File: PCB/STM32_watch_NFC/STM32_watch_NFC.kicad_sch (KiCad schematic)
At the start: 54 parts, among them J1 Conn_01x06_Socket, Q1 2N7000, SW1 SW_DPST_x2, SW2 SW_DPST_x2, SW3 SW_DPST_x2, U1 STM32L031G6Ux, Y2 32.768kHz

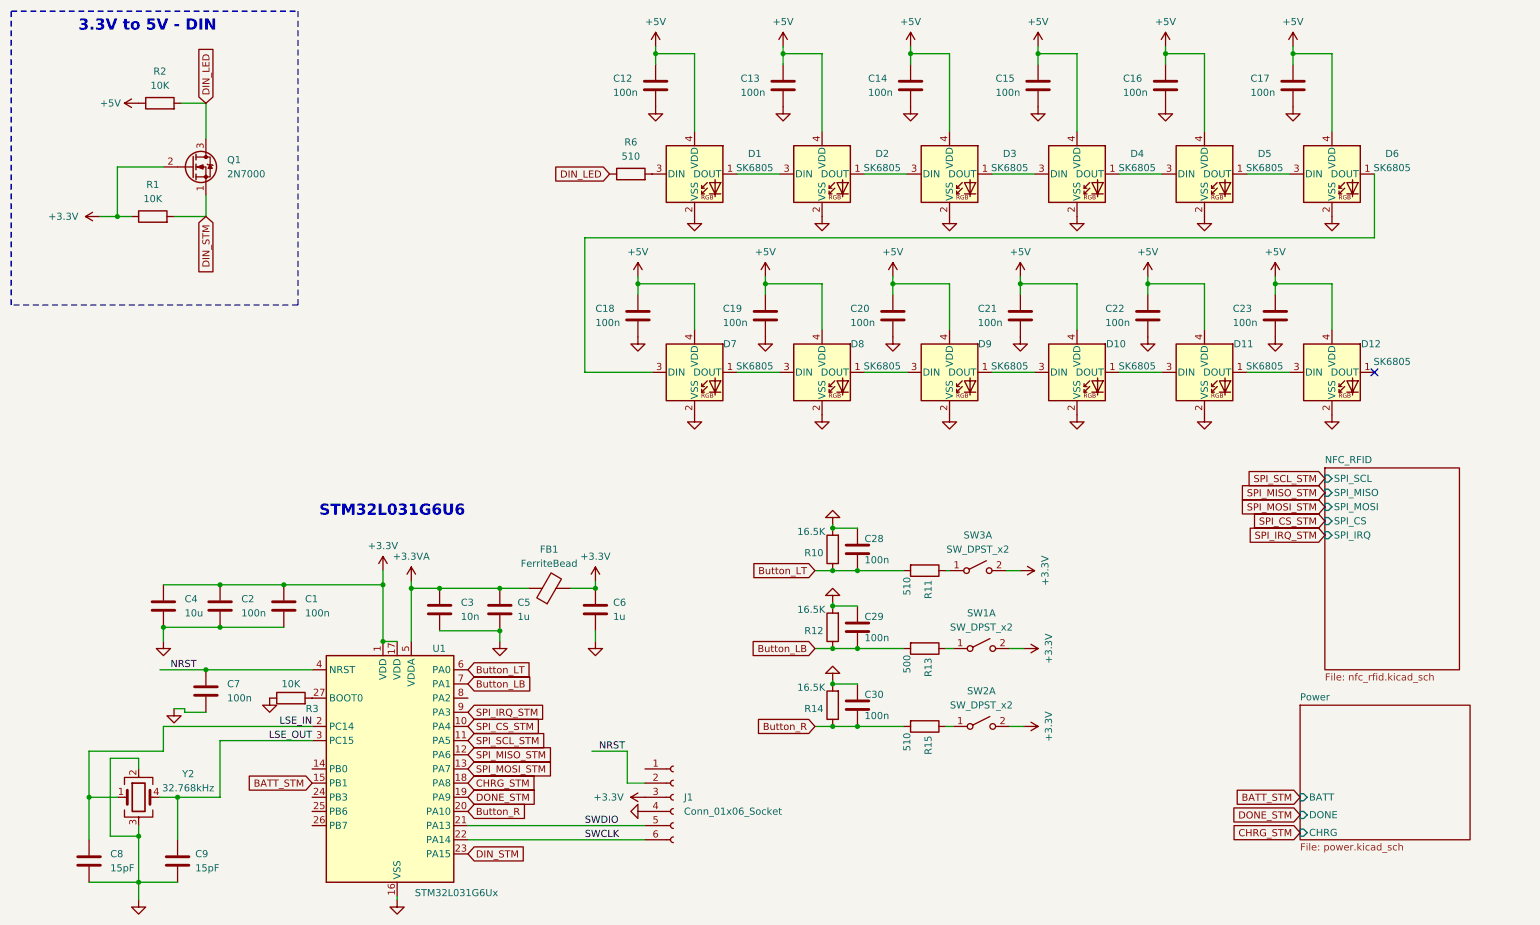
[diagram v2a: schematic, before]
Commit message: Kicad - layout
I placed all components in logical way. It is NOT routed.
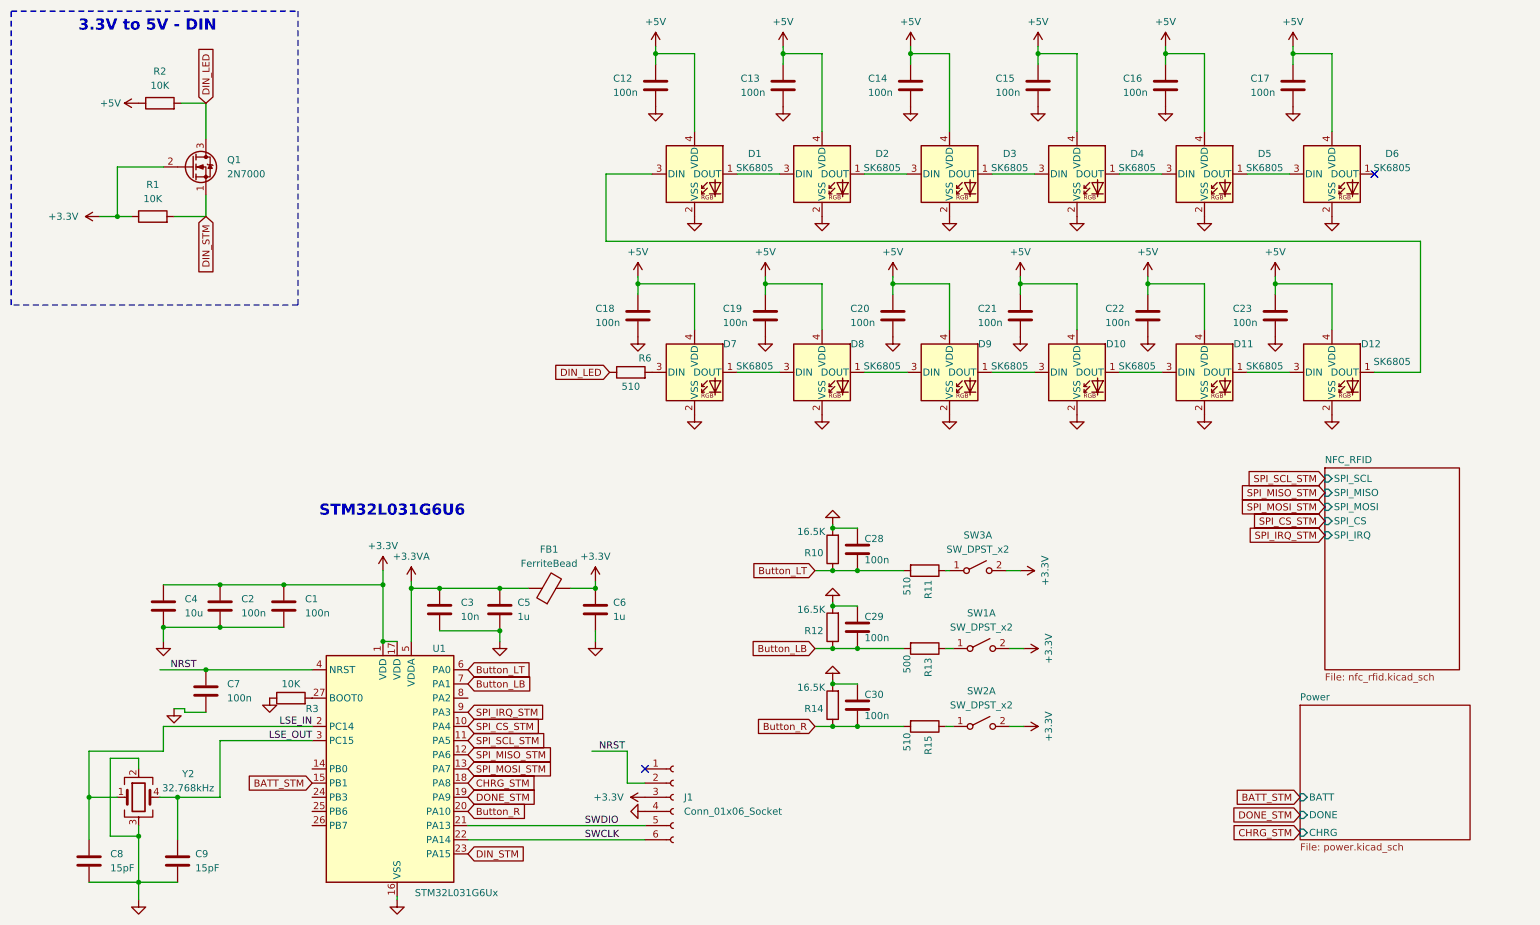
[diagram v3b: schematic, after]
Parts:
- C3: footprint Capacitor_SMD:C_0201_0603Metric -> Capacitor_SMD:C_0402_1005Metric; LCSC C541216 -> C323592
- J1: footprint Connector_JST:JST_SUR_SM05B-SURS-TF_1x05-1MP_P0.80mm_Horizontal -> Connector_JST:JST_SUR_SM06B-SURS-TF_1x06-1MP_P0.80mm_Horizontal
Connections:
- net at D6.1 (DOUT): no longer D7.3 (DIN)
- net at D12.1 (DOUT): now also D1.3 (DIN)
- net at R6.2: now also D7.3 (DIN); no longer D1.3 (DIN)
- no-connect marks 1 -> 2
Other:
- moved on the sheet: R6
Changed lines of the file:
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@@
   (junction (at 31.115 48.895) (diameter 0) (color 0 0 0 0)
   )
-  (no_connect (at 256.54 76.835))
+  (no_connect (at 256.54 41.275))
+  (no_connect (at 125.73 147.955))
   (wire (pts (xy 210.82 76.835) (xy 218.44 76.835))
     (stroke (width 0) (type default))
@@
     (stroke (width 0) (type default))
   )
-  (wire (pts (xy 114.935 52.705) (xy 114.935 76.835))
-    (stroke (width 0) (type default))
-  )
   (wire (pts (xy 203.2 33.655) (xy 203.2 19.685))
     (stroke (width 0) (type default))
@@
     (stroke (width 0) (type default))
   )
-  (wire (pts (xy 256.54 41.275) (xy 256.54 52.705))
+  (wire (pts (xy 256.54 76.835) (xy 264.795 76.835))
     (stroke (width 0) (type default))
   )
@@
     (stroke (width 0) (type default))
   )
+  (wire (pts (xy 118.745 53.34) (xy 118.745 41.275))
+    (stroke (width 0) (type default))
+  )
   (wire (pts (xy 226.06 33.655) (xy 226.06 19.685))
     (stroke (width 0) (type default))
@@
     (stroke (width 0) (type default))
   )
+  (wire (pts (xy 264.795 76.835) (xy 264.795 53.34))
+    (stroke (width 0) (type default))
+  )
   (wire (pts (xy 163.83 140.335) (xy 172.085 140.335))
     (stroke (width 0) (type default))
@@
     (stroke (width 0) (type default))
   )
-  (wire (pts (xy 114.935 76.835) (xy 127 76.835))
-    (stroke (width 0) (type default))
-  )
   (wire (pts (xy 124.46 59.69) (xy 124.46 60.96))
     (stroke (width 0) (type default))
@@
     (stroke (width 0) (type default))
   )
-  (wire (pts (xy 256.54 52.705) (xy 114.935 52.705))
-    (stroke (width 0) (type default))
-  )
   (wire (pts (xy 187.96 76.835) (xy 195.58 76.835))
     (stroke (width 0) (type default))
@@
     (stroke (width 0) (type default))
   )
+  (wire (pts (xy 264.795 53.34) (xy 118.745 53.34))
+    (stroke (width 0) (type default))
+  )
   (wire (pts (xy 29.845 160.02) (xy 29.845 146.05))
     (stroke (width 0) (type default))
@@
   )
   (wire (pts (xy 34.925 160.02) (xy 34.925 168.275))
+    (stroke (width 0) (type default))
+  )
+  (wire (pts (xy 118.745 41.275) (xy 127 41.275))
     (stroke (width 0) (type default))
   )
@@
     )
   )
-  (global_label "DIN_LED" (shape input) (at 119.38 41.275 180) (fields_autoplaced)
+  (global_label "DIN_LED" (shape input) (at 119.38 76.835 180) (fields_autoplaced)
     (effects (font (size 1.27 1.27)) (justify right))
-    (property "Intersheetrefs" "${INTERSHEET_REFS}" (at 108.7748 41.275 0)
+    (property "Intersheetrefs" "${INTERSHEET_REFS}" (at 108.7748 76.835 0)
       (effects (font (size 1.27 1.27)) (justify right) hide)
     )
@@
       (effects (font (size 1.27 1.27)) (justify left))
     )
-    (property "Footprint" "Connector_JST:JST_SUR_SM05B-SURS-TF_1x05-1MP_P0.80mm_Horizontal" (at 130.81 153.035 0)
+    (property "Footprint" "Connector_JST:JST_SUR_SM06B-SURS-TF_1x06-1MP_P0.80mm_Horizontal" (at 130.81 153.035 0)
       (effects (font (size 1.27 1.27)) hide)
     )
@@
       (effects (font (size 1.27 1.27)) (justify left))
     )
-    (property "Footprint" "Capacitor_SMD:C_0201_0603Metric" (at 89.8652 123.19 0)
+    (property "Footprint" "Capacitor_SMD:C_0402_1005Metric" (at 89.8652 123.19 0)
       (effects (font (size 1.27 1.27)) hide)
     )
@@
       (effects (font (size 1.27 1.27)) hide)
     )
-    (property "LCSC" "C541216" (at 88.9 119.38 0)
+    (property "LCSC" "C323592" (at 88.9 119.38 0)
       (effects (font (size 1.27 1.27)) hide)
     )
@@
     )
   )
-  (symbol (lib_id "Device:R") (at 123.19 41.275 90) (unit 1)
-    (in_bom yes) (on_board yes) (dnp no) (fields_autoplaced)
-    (property "Reference" "R6" (at 123.19 35.56 90)
-      (effects (font (size 1.27 1.27)))
-    )
-    (property "Value" "510" (at 123.19 38.1 90)
-      (effects (font (size 1.27 1.27)))
-    )
-    (property "Footprint" "Resistor_SMD:R_0402_1005Metric" (at 123.19 43.053 90)
-      (effects (font (size 1.27 1.27)) hide)
-    )
-    (property "Datasheet" "~" (at 123.19 41.275 0)
-      (effects (font (size 1.27 1.27)) hide)
-    )
-    (property "LCSC" "C103085" (at 123.19 41.275 90)
-      (effects (font (size 1.27 1.27)) hide)
-    )
+  (symbol (lib_id "Device:R") (at 123.19 76.835 90) (unit 1)
+    (in_bom yes) (on_board yes) (dnp no)
+    (property "Reference" "R6" (at 125.73 74.295 90)
+      (effects (font (size 1.27 1.27)))
+    )
+    (property "Value" "510" (at 123.19 79.375 90)
+      (effects (font (size 1.27 1.27)))
+    )
+    (property "Footprint" "Resistor_SMD:R_0402_1005Metric" (at 123.19 78.613 90)
+      (effects (font (size 1.27 1.27)) hide)
+    )
+    (property "Datasheet" "~" (at 123.19 76.835 0)
+      (effects (font (size 1.27 1.27)) hide)
+    )
+    (property "LCSC" "C103085" (at 123.19 76.835 90)
+      (effects (font (size 1.27 1.27)) hide)
+    )

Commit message: Kicad - Routing 4
Completed version. I just need to add graphics :)
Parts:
- added 3V3: 3V3, TestPoint:TestPoint_Pad_D1.5mm, symbol Connector:TestPoint
- added CLK1, DINS1, DIO1: ~, TestPoint:TestPoint_Pad_D1.0mm, symbol Connector:TestPoint
- added GND1: GND, TestPoint:TestPoint_Pad_D1.5mm, symbol Connector:TestPoint
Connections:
- net +3.3V: now also 3V3.1
- net DIN_STM: now also DINS1.1
- net GND: now also GND1.1
- net SWCLK: now also CLK1.1
- net SWDIO: now also DIO1.1
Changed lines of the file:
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@@
   (junction (at 238.76 60.96) (diameter 0) (color 0 0 0 0)
   )
+  (junction (at 125.73 160.655) (diameter 0) (color 0 0 0 0)
+  )
+  (junction (at 46.99 47.625) (diameter 0) (color 0 0 0 0)
+  )
   (junction (at 78.74 125.095) (diameter 0) (color 0 0 0 0)
   )
@@
   (junction (at 99.695 115.57) (diameter 0) (color 0 0 0 0)
   )
+  (junction (at 116.84 124.46) (diameter 0) (color 0 0 0 0)
+  )
+  (junction (at 64.77 114.935) (diameter 0) (color 0 0 0 0)
+  )
   (junction (at 49.53 122.555) (diameter 0) (color 0 0 0 0)
   )
@@
   (junction (at 34.925 160.02) (diameter 0) (color 0 0 0 0)
   )
+  (junction (at 111.76 158.115) (diameter 0) (color 0 0 0 0)
+  )
   (junction (at 147.32 60.96) (diameter 0) (color 0 0 0 0)
   )
@@
     (stroke (width 0) (type default))
   )
+  (wire (pts (xy 116.84 124.46) (xy 116.84 125.095))
+    (stroke (width 0) (type default))
+  )
   (wire (pts (xy 150.495 18.415) (xy 150.495 19.685))
     (stroke (width 0) (type default))
@@
     (stroke (width 0) (type default))
   )
-  (wire (pts (xy 93.98 158.115) (xy 125.73 158.115))
+  (wire (pts (xy 93.98 158.115) (xy 111.76 158.115))
     (stroke (width 0) (type default))
   )
@@
     (stroke (width 0) (type default))
   )
-  (wire (pts (xy 46.99 45.085) (xy 46.99 48.895))
+  (wire (pts (xy 46.99 45.085) (xy 46.99 47.625))
     (stroke (width 0) (type default))
   )
@@
     (stroke (width 0) (type default))
   )
-  (wire (pts (xy 116.84 123.19) (xy 116.84 125.095))
+  (wire (pts (xy 116.84 123.19) (xy 116.84 124.46))
     (stroke (width 0) (type default))
   )
@@
     (stroke (width 0) (type default))
   )
-  (wire (pts (xy 60.96 114.935) (xy 78.74 114.935))
+  (wire (pts (xy 60.96 114.935) (xy 64.77 114.935))
     (stroke (width 0) (type default))
   )
@@
     (stroke (width 0) (type default))
   )
+  (wire (pts (xy 46.99 47.625) (xy 46.99 48.895))
+    (stroke (width 0) (type default))
+  )
   (wire (pts (xy 78.74 125.095) (xy 81.28 125.095))
     (stroke (width 0) (type default))
@@
     (stroke (width 0) (type default))
   )
+  (wire (pts (xy 64.77 114.935) (xy 78.74 114.935))
+    (stroke (width 0) (type default))
+  )
   (wire (pts (xy 187.96 41.275) (xy 195.58 41.275))
     (stroke (width 0) (type default))
@@
     (stroke (width 0) (type default))
   )
+  (wire (pts (xy 111.76 158.115) (xy 125.73 158.115))
+    (stroke (width 0) (type default))
+  )
   (wire (pts (xy 170.18 60.96) (xy 180.34 60.96))
     (stroke (width 0) (type default))
@@
     )
   )
+  (symbol (lib_id "Connector:TestPoint") (at 125.73 160.655 180) (unit 1)
+    (in_bom yes) (on_board yes) (dnp no)
+    (property "Reference" "CLK1" (at 127 165.1 90)
+      (effects (font (size 1.27 1.27)) (justify left))
+    )
+    (property "Value" "~" (at 135.255 165.1 0)
+      (effects (font (size 1.27 1.27)) (justify left))
+    )
+    (property "Footprint" "TestPoint:TestPoint_Pad_D1.0mm" (at 120.65 160.655 0)
+      (effects (font (size 1.27 1.27)) hide)
+    )
+    (property "Datasheet" "~" (at 120.65 160.655 0)
+      (effects (font (size 1.27 1.27)) hide)
+    )
+    (pin "1")
+    (instances
+      (project "STM32_watch_NFC"
+        (path "/e445874f-c7a3-43dd-b930-6bce1d4fa2ef"
+          (reference "CLK1") (unit 1)
+        )
+      )
+    )
+  )
   (symbol (lib_id "Device:R") (at 159.385 108.585 180) (unit 1)
     (in_bom yes) (on_board yes) (dnp no)
@@
     )
   )
+  (symbol (lib_id "Connector:TestPoint") (at 111.76 158.115 0) (unit 1)
+    (in_bom yes) (on_board yes) (dnp no)
+    (property "Reference" "DIO1" (at 110.49 153.67 90)
+      (effects (font (size 1.27 1.27)) (justify left))
+    )
+    (property "Value" "~" (at 102.235 153.67 0)
+      (effects (font (size 1.27 1.27)) (justify left))
+    )
+    (property "Footprint" "TestPoint:TestPoint_Pad_D1.0mm" (at 116.84 158.115 0)
+      (effects (font (size 1.27 1.27)) hide)
+    )
+    (property "Datasheet" "~" (at 116.84 158.115 0)
+      (effects (font (size 1.27 1.27)) hide)
+    )
+    (pin "1")
+    (instances
+      (project "STM32_watch_NFC"
+        (path "/e445874f-c7a3-43dd-b930-6bce1d4fa2ef"
+          (reference "DIO1") (unit 1)
+        )
+      )
+    )
+  )
   (symbol (lib_id "power:GND") (at 170.18 70.485 0) (unit 1)
     (in_bom yes) (on_board yes) (dnp no) (fields_autoplaced)
@@
     )
   )
+  (symbol (lib_id "Connector:TestPoint") (at 116.84 124.46 270) (unit 1)
+    (in_bom yes) (on_board yes) (dnp no) (fields_autoplaced)
+    (property "Reference" "GND1" (at 122.555 123.19 90)
+      (effects (font (size 1.27 1.27)) (justify left))
+    )
+    (property "Value" "GND" (at 122.555 125.73 90)
+      (effects (font (size 1.27 1.27)) (justify left))
+    )
+    (property "Footprint" "TestPoint:TestPoint_Pad_D1.5mm" (at 116.84 129.54 0)
+      (effects (font (size 1.27 1.27)) hide)
+    )
+    (property "Datasheet" "~" (at 116.84 129.54 0)
+      (effects (font (size 1.27 1.27)) hide)
+    )
+    (pin "1")
+    (instances
+      (project "STM32_watch_NFC"
+        (path "/e445874f-c7a3-43dd-b930-6bce1d4fa2ef"
+          (reference "GND1") (unit 1)
+        )
+      )
+    )
+  )
   (symbol (lib_id "power:+5V") (at 219.075 18.415 0) (unit 1)
     (in_bom yes) (on_board yes) (dnp no) (fields_autoplaced)
@@
     )
   )
+  (symbol (lib_id "Connector:TestPoint") (at 46.99 47.625 270) (unit 1)
+    (in_bom yes) (on_board yes) (dnp no)
+    (property "Reference" "DINS1" (at 51.435 46.355 90)
+      (effects (font (size 1.27 1.27)) (justify left))
+    )
+    (property "Value" "~" (at 51.435 38.1 0)
+      (effects (font (size 1.27 1.27)) (justify left))
+    )
+    (property "Footprint" "TestPoint:TestPoint_Pad_D1.0mm" (at 46.99 52.705 0)
+      (effects (font (size 1.27 1.27)) hide)
+    )
+    (property "Datasheet" "~" (at 46.99 52.705 0)
+      (effects (font (size 1.27 1.27)) hide)
+    )
+    (pin "1")
+    (instances
+      (project "STM32_watch_NFC"
+        (path "/e445874f-c7a3-43dd-b930-6bce1d4fa2ef"
+          (reference "DINS1") (unit 1)
+        )
+      )
+    )
+  )
   (symbol (lib_id "power:GND") (at 180.34 84.455 0) (unit 1)
     (in_bom yes) (on_board yes) (dnp no) (fields_autoplaced)
@@
         )
       )
+    )
+  )
+  (symbol (lib_id "Connector:TestPoint") (at 64.77 114.935 0) (unit 1)
+    (in_bom yes) (on_board yes) (dnp no) (fields_autoplaced)
+    (property "Reference" "3V3" (at 67.31 110.363 0)
+      (effects (font (size 1.27 1.27)) (justify left))
+    )
+    (property "Value" "3V3" (at 67.31 112.903 0)
+      (effects (font (size 1.27 1.27)) (justify left))
+    )
+    (property "Footprint" "TestPoint:TestPoint_Pad_D1.5mm" (at 69.85 114.935 0)
+      (effects (font (size 1.27 1.27)) hide)
+    )
+    (property "Datasheet" "~" (at 69.85 114.935 0)
+      (effects (font (size 1.27 1.27)) hide)
+    )
+    (pin "1")
+    (instances
+      (project "STM32_watch_NFC"
+        (path "/e445874f-c7a3-43dd-b930-6bce1d4fa2ef"
+          (reference "3V3") (unit 1)
+        )
+      )

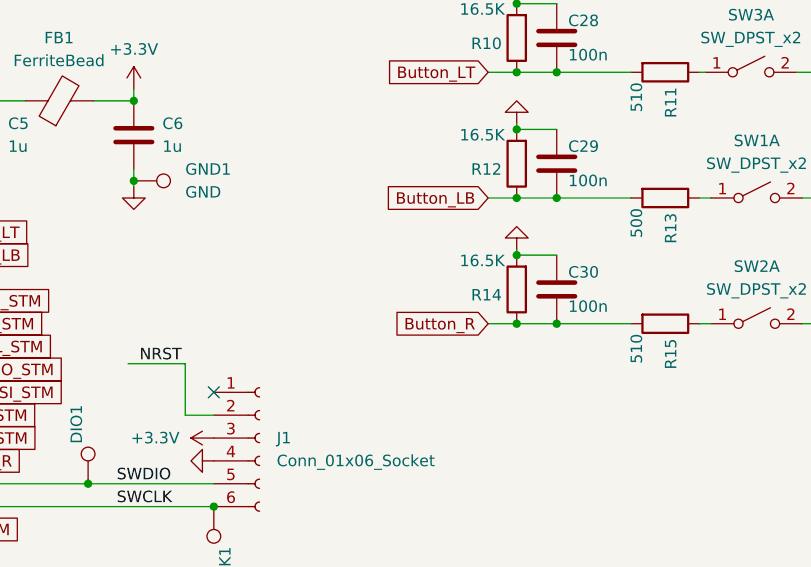
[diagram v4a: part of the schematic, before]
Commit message: Coding LEDs
Library for led management, buttons
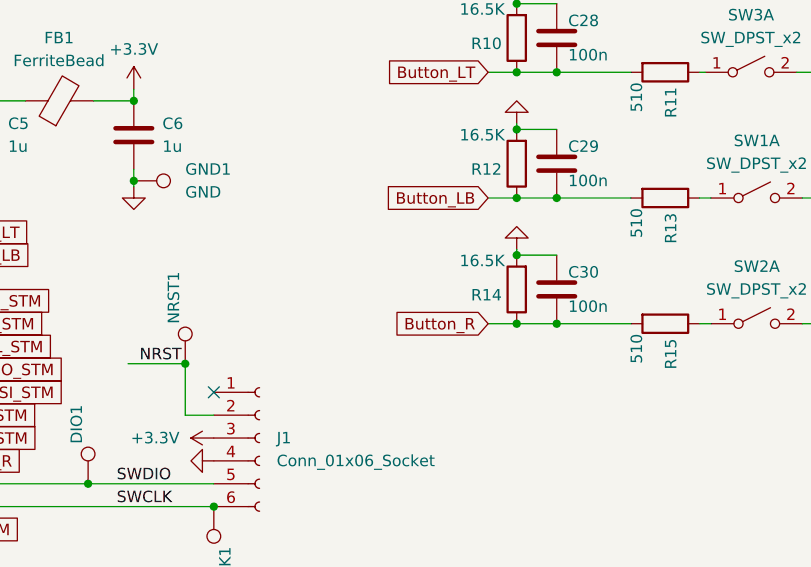
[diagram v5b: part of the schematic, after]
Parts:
- added NRST1: ~, TestPoint:TestPoint_Pad_D1.0mm, symbol Connector:TestPoint
- J1: LCSC (none) -> C495545
- R10: footprint Resistor_SMD:R_0402_1005Metric -> Resistor_SMD:R_0805_2012Metric
- R13: value 500 -> 510
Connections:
- net NRST: now also NRST1.1
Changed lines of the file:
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@@
   (junction (at 31.115 48.895) (diameter 0) (color 0 0 0 0)
   )
+  (junction (at 122.555 144.78) (diameter 0) (color 0 0 0 0)
+  )
   (no_connect (at 256.54 41.275))
   (no_connect (at 125.73 147.955))
@@
       (effects (font (size 1.27 1.27)) hide)
     )
+    (property "LCSC" "C495545" (at 130.81 153.035 0)
+      (effects (font (size 1.27 1.27)) hide)
+    )
     (pin "3")
     (pin "2")
@@
       (effects (font (size 1.27 1.27)) (justify right))
     )
-    (property "Value" "500" (at 172.72 130.81 0)
+    (property "Value" "510" (at 172.72 130.81 0)
       (effects (font (size 1.27 1.27)) (justify right))
     )
@@
       (effects (font (size 1.27 1.27)) (justify right))
     )
-    (property "Footprint" "Resistor_SMD:R_0402_1005Metric" (at 161.163 108.585 90)
+    (property "Footprint" "Resistor_SMD:R_0805_2012Metric" (at 161.163 108.585 90)
       (effects (font (size 1.27 1.27)) hide)
     )
@@
         )
       )
+    )
+  )
+  (symbol (lib_id "Connector:TestPoint") (at 122.555 144.78 0) (unit 1)
+    (in_bom yes) (on_board yes) (dnp no)
+    (property "Reference" "NRST1" (at 121.285 140.335 90)
+      (effects (font (size 1.27 1.27)) (justify left))
+    )
+    (property "Value" "~" (at 113.03 140.335 0)
+      (effects (font (size 1.27 1.27)) (justify left))
+    )
+    (property "Footprint" "TestPoint:TestPoint_Pad_D1.0mm" (at 127.635 144.78 0)
+      (effects (font (size 1.27 1.27)) hide)
+    )
+    (property "Datasheet" "~" (at 127.635 144.78 0)
+      (effects (font (size 1.27 1.27)) hide)
+    )
+    (pin "1")
+    (instances
+      (project "STM32_watch_NFC"
+        (path "/e445874f-c7a3-43dd-b930-6bce1d4fa2ef"
+          (reference "NRST1") (unit 1)
+        )
+      )
